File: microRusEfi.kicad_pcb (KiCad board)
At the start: 2 copper layers, 80.6 x 93.7 mm, 236 parts, among them CN14 10nF, CN17 10nF, CN5 10nF, CN6 10nF, J1 USB_B_Micro, J2 Conn_02x05_Odd_Even, J3 Conn_01x02, J4 Conn_02x05_Counter_Clockwise, Q1 IPD30N06S2L-23, SW1 SW_Push, SW2 SW_Push, U1 STM32F407VGT6, U11 IS25LP256D-xM, U2 TLE8888QK, U3 Molex_48_pin, U31 MIC4427, U32 MIC4427, U33 MIC4427, U35 MCP6004, U36 MCP6004, U4 TLE9201SG, U46 MCP6004, U5 LM1117-3.3, U6 W25QxxJVS, U7 XC6206 3.3V, U8 MCP6004, X1 8MHz 20pF, Y2 32768 Hz

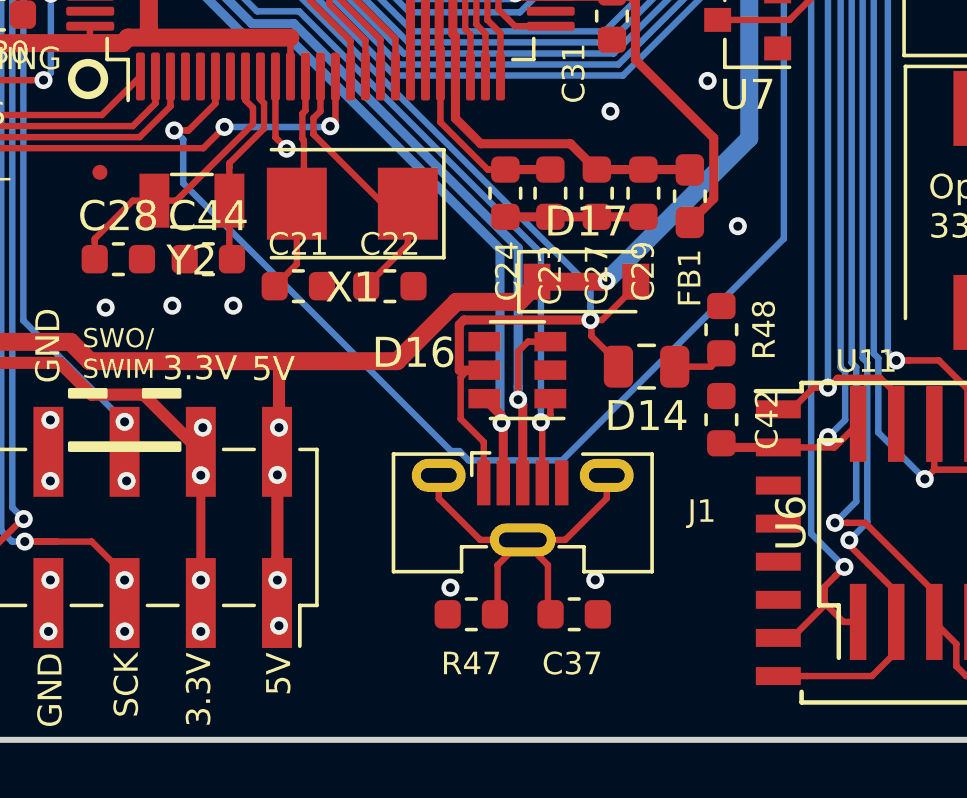
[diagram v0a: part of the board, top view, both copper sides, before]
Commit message: Replace micro USB connector with through hole version
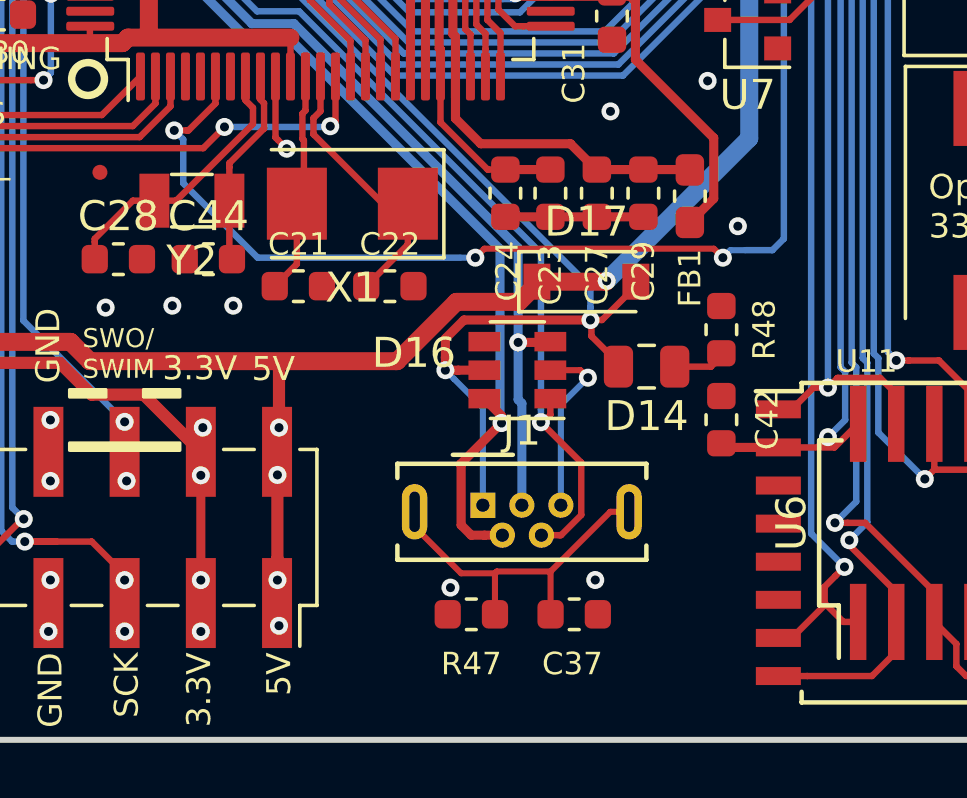
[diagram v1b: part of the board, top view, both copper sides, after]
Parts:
- J1: footprint Connector_USB:USB_Micro-B_Molex-105133-0031 -> Connectors_USB:USB_Micro-B_Wuerth-614105150721_Vertical
- moved J1 1.33 mm to (59.5, 108.2)
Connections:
- net /TLE8888-1QK/DFB12 renamed Net-(U2-Pad78)
- net /TLE8888-1QK/DFB13 renamed Net-(U2-Pad80)
- U2 pad 76: /AV9 -> Net-(U2-Pad76)
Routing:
- net GND: track 46.5 -> 52.4 mm, vias 117 -> 118
- net /MCU/VBAT: track 44.4 -> 39.1 mm, vias 1 -> 3
- net /USB_D-: track 91.0 -> 94.4 mm
- net /MCU/PA10: track 35.4 -> 38.7 mm
- net /MCU/shield: track 13.9 -> 11.9 mm
- net /USB_D+: track 87.2 -> 86.2 mm
- net /MCU/PA9: track 41.7 -> 42.6 mm, vias 2 -> 3

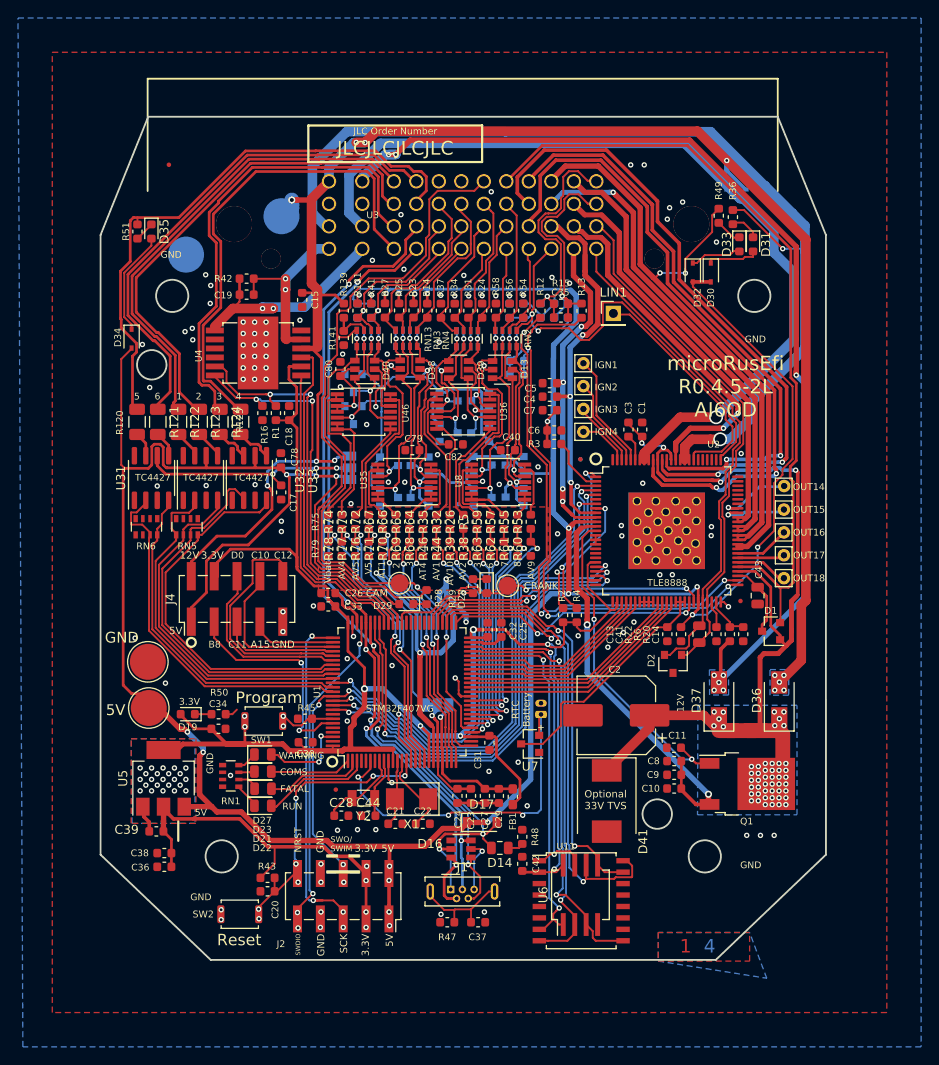
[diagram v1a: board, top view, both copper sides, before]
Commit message: Use mounting hole components on PCB instead of vias with filled zones
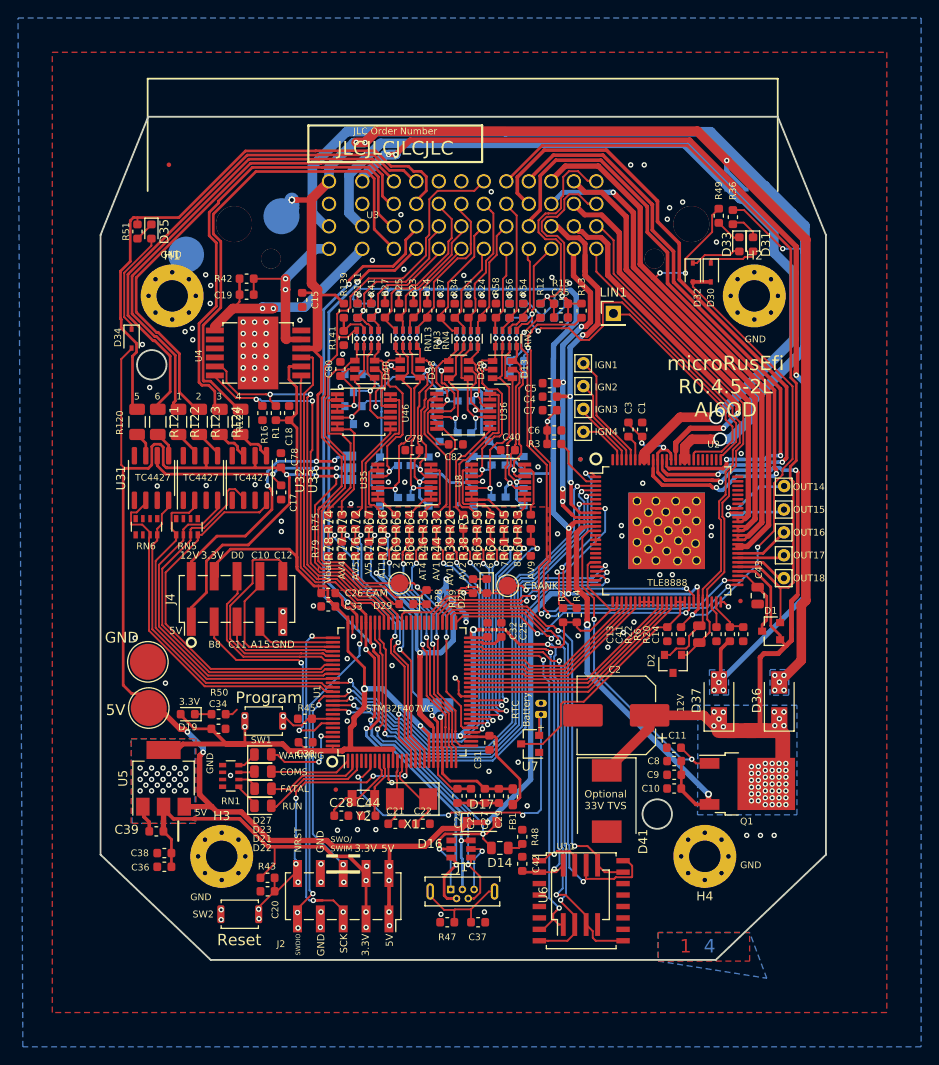
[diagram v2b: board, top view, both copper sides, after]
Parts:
- added H1: MountingHole, Mounting_Holes:MountingHole_3.5mm_Pad_Via, F.Cu at (28.6, 42.3)
- added H2: MountingHole, Mounting_Holes:MountingHole_3.5mm_Pad_Via, F.Cu at (93.2, 42.3)
- added H3: MountingHole, Mounting_Holes:MountingHole_3.5mm_Pad_Via, F.Cu at (34.1, 104.6)
- added H4: MountingHole, Mounting_Holes:MountingHole_3.5mm_Pad_Via, F.Cu at (87.7, 104.6)
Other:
- outline, holes or cut-outs redrawn

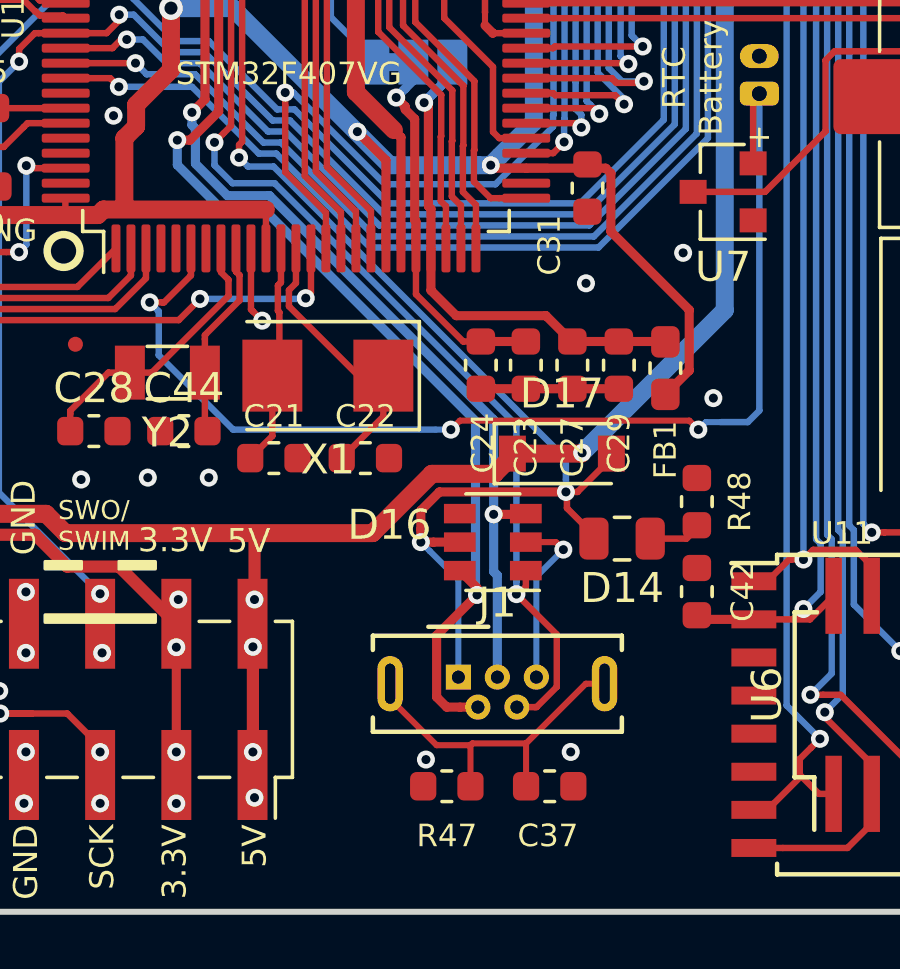
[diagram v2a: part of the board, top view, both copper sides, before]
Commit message: Rotate USB connector to follow wide-side-down orientation expectation.
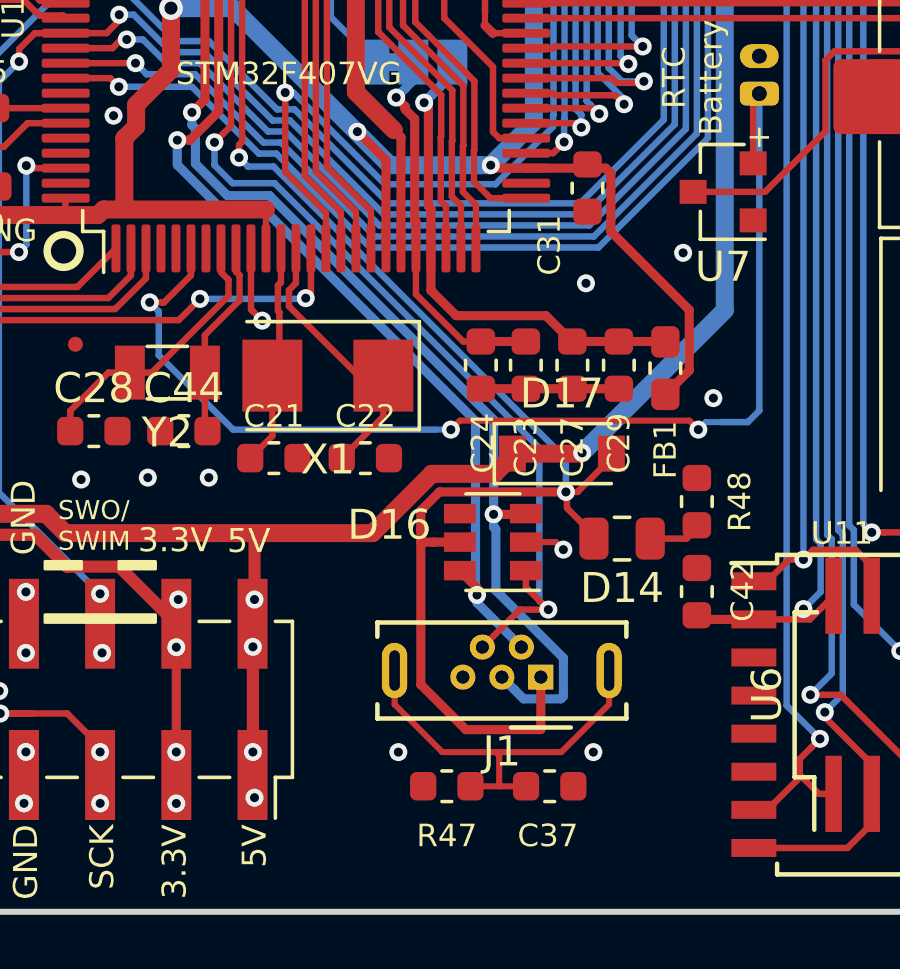
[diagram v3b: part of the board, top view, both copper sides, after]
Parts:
- moved J1 2.75 mm to (62.2, 108.2), turned to 180 degrees
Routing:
- net /MCU/PA9: track 42.6 -> 48.7 mm, vias 3 -> 2
- net GND: track 52.4 -> 47.8 mm
- net /USB_D+: track 86.2 -> 90.1 mm
- net /USB_D-: track 94.4 -> 91.3 mm
- net /MCU/shield: track 11.9 -> 13.8 mm
- net /MCU/PA10: track 38.7 -> 37.7 mm
